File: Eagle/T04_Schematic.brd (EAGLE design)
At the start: 40.6 x 63.5 mm, 30 parts

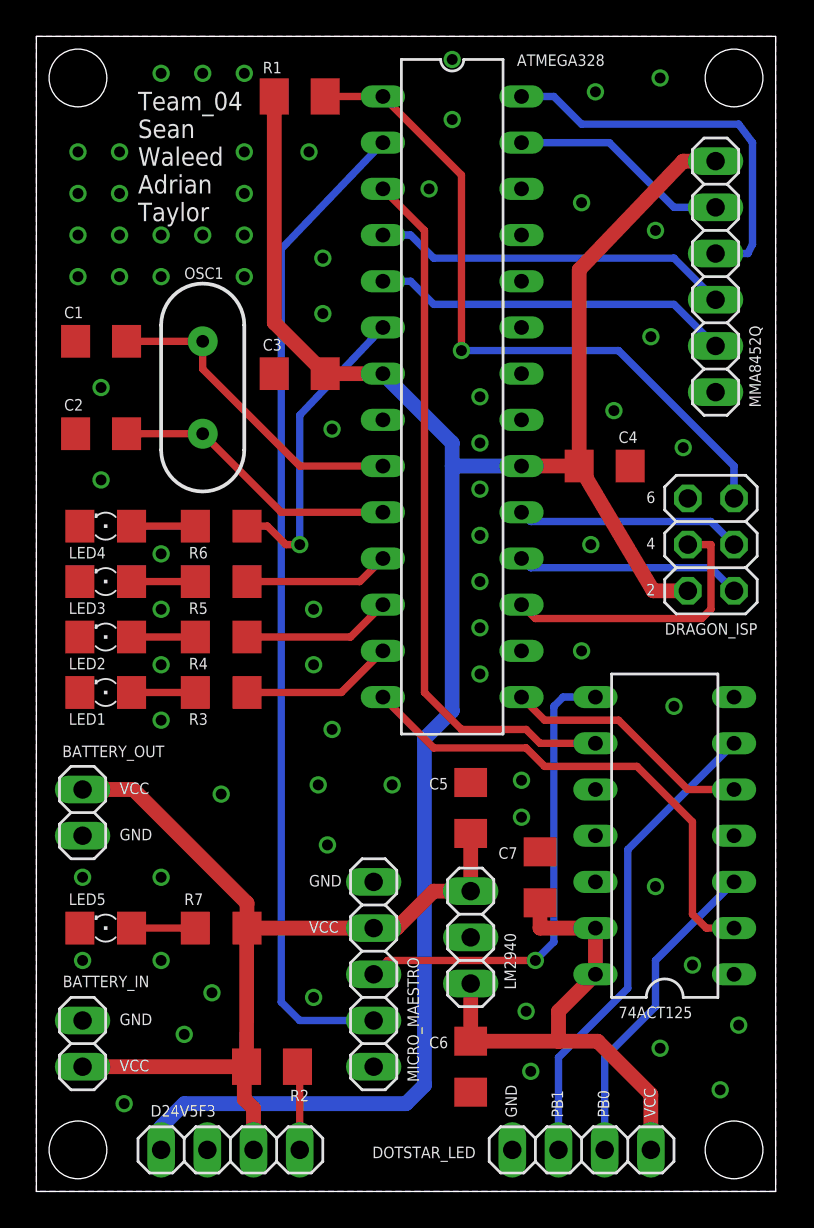
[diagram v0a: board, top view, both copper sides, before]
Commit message: Minor Changes for OSHPark -- PRINTED
Moved vias and text to make it pretty.
-- This File Uploaded to Print!!!
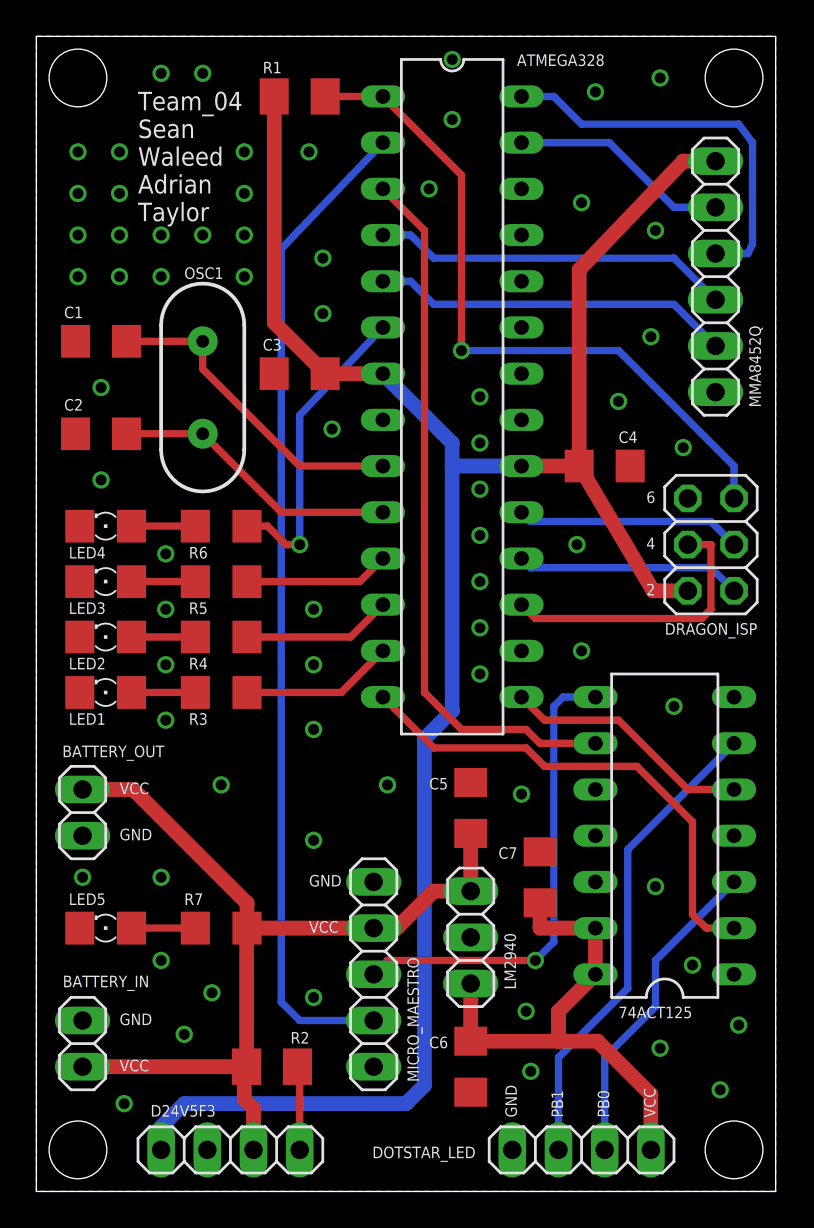
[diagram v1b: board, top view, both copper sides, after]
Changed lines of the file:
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@@
 </element>
 <element name="R2" library="rcl" package="M1206" value="10K" x="12.954" y="6.858" smashed="yes" rot="R180">
-<attribute name="NAME" x="14.986" y="5.588" size="0.635" layer="25" rot="R180"/>
+<attribute name="NAME" x="13.97" y="8.128" size="0.635" layer="25"/>
 <attribute name="VALUE" x="14.224" y="4.318" size="0.6096" layer="27"/>
 </element>
@@
 <via x="6.858" y="61.468" extent="1-16" drill="0.6"/>
 <via x="9.144" y="61.468" extent="1-16" drill="0.6"/>
-<via x="11.43" y="61.468" extent="1-16" drill="0.6"/>
+<wire x1="11.43" y1="61.468" x2="11.43" y2="61.468" width="0" layer="19" extent="1-16"/>
 <via x="11.43" y="50.292" extent="1-16" drill="0.6"/>
 <via x="3.556" y="44.196" extent="1-16" drill="0.6"/>
 <via x="3.556" y="39.116" extent="1-16" drill="0.6"/>
-<via x="6.858" y="35.052" extent="1-16" drill="0.6"/>
-<via x="6.858" y="32.004" extent="1-16" drill="0.6"/>
-<via x="6.858" y="28.956" extent="1-16" drill="0.6"/>
-<via x="6.858" y="25.908" extent="1-16" drill="0.6"/>
+<via x="7.112" y="35.052" extent="1-16" drill="0.6"/>
+<via x="7.112" y="32.004" extent="1-16" drill="0.6"/>
+<via x="7.112" y="28.956" extent="1-16" drill="0.6"/>
+<via x="7.112" y="25.908" extent="1-16" drill="0.6"/>
 <via x="2.54" y="17.272" extent="1-16" drill="0.6"/>
-<via x="2.54" y="12.7" extent="1-16" drill="0.6"/>
+<wire x1="2.54" y1="12.7" x2="2.54" y2="12.7" width="0" layer="19" extent="1-16"/>
 <via x="6.858" y="17.272" extent="1-16" drill="0.6"/>
 <via x="6.858" y="12.7" extent="1-16" drill="0.6"/>
@@
 <via x="26.924" y="9.906" extent="1-16" drill="0.6"/>
 <via x="37.592" y="5.588" extent="1-16" drill="0.6"/>
-<via x="10.16" y="21.844" extent="1-16" drill="0.6"/>
-<via x="19.558" y="22.352" extent="1-16" drill="0.6"/>
+<via x="10.16" y="22.352" extent="1-16" drill="0.6"/>
+<via x="19.304" y="22.352" extent="1-16" drill="0.6"/>
 <via x="24.384" y="41.148" extent="1-16" drill="0.6"/>
-<via x="31.75" y="42.926" extent="1-16" drill="0.6"/>
-<via x="30.48" y="35.56" extent="1-16" drill="0.6"/>
+<via x="32.004" y="43.434" extent="1-16" drill="0.6"/>
+<via x="29.718" y="35.56" extent="1-16" drill="0.6"/>
 <via x="33.782" y="46.99" extent="1-16" drill="0.6"/>
 <via x="29.972" y="54.356" extent="1-16" drill="0.6"/>
@@
 <via x="15.24" y="32.004" extent="1-16" drill="0.6"/>
 <via x="15.24" y="28.956" extent="1-16" drill="0.6"/>
-<via x="16.256" y="25.4" extent="1-16" drill="0.6"/>
+<via x="15.24" y="25.4" extent="1-16" drill="0.6"/>
 <via x="15.24" y="10.668" extent="1-16" drill="0.6"/>
-<via x="16.002" y="19.05" extent="1-16" drill="0.6"/>
+<via x="15.24" y="19.304" extent="1-16" drill="0.6"/>
 <contactref element="74ACT125" pad="11"/>
 <contactref element="74ACT125" pad="12"/>
@@
 <via x="34.036" y="52.832" extent="1-16" drill="0.6"/>
 <via x="21.59" y="55.118" extent="1-16" drill="0.6"/>
-<via x="15.494" y="22.352" extent="1-16" drill="0.6"/>
-<via x="26.67" y="20.574" extent="1-16" drill="0.6"/>
+<wire x1="15.24" y1="22.352" x2="15.24" y2="22.352" width="0" layer="19" extent="1-16"/>
+<wire x1="26.67" y1="20.574" x2="26.67" y2="20.574" width="0" layer="19" extent="1-16"/>
 <via x="35.052" y="26.67" extent="1-16" drill="0.6"/>
 <via x="34.036" y="16.764" extent="1-16" drill="0.6"/>
 <via x="38.608" y="9.144" extent="1-16" drill="0.6"/>
-<via x="26.67" y="22.606" extent="1-16" drill="0.6"/>
+<via x="26.67" y="21.844" extent="1-16" drill="0.6"/>
 <contactref element="C7" pad="2"/>
 <via x="34.29" y="7.874" extent="1-16" drill="0.6"/>

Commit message: Added Resistor and LED Voltages
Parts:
- LED1: value TBD Voltage -> G - 2.1V
- LED2, LED3: value TBD Voltage -> Y - 2.2V
- LED4: value TBD Voltage -> R - 1.7V
- LED5: value TBD Voltage -> B - 3.2V
- R3: value TBD Resistance -> 68 Ohms
- R4, R5: value TBD Resistance -> 56 Ohms
- R6: value TBD Resistance -> 82 Ohms
- R7: value TBD Resistance -> 150 Ohms
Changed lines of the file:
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@@
 <attribute name="NAME" x="34.544" y="30.607" size="0.635" layer="25" ratio="10"/>
 </element>
-<element name="LED1" library="led" package="1206" value="TBD Voltage" x="3.81" y="27.432" smashed="yes" rot="R180">
+<element name="LED1" library="led" package="1206" value="G - 2.1V" x="3.81" y="27.432" smashed="yes" rot="R180">
 <attribute name="NAME" x="1.778" y="25.654" size="0.635" layer="25"/>
 </element>
-<element name="LED2" library="led" package="1206" value="TBD Voltage" x="3.81" y="30.48" smashed="yes" rot="R180">
+<element name="LED2" library="led" package="1206" value="Y - 2.2V" x="3.81" y="30.48" smashed="yes" rot="R180">
 <attribute name="NAME" x="1.778" y="28.702" size="0.635" layer="25"/>
 </element>
-<element name="LED3" library="led" package="1206" value="TBD Voltage" x="3.81" y="33.528" smashed="yes" rot="R180">
+<element name="LED3" library="led" package="1206" value="Y - 2.2V" x="3.81" y="33.528" smashed="yes" rot="R180">
 <attribute name="NAME" x="1.778" y="31.75" size="0.635" layer="25"/>
 </element>
-<element name="LED4" library="led" package="1206" value="TBD Voltage" x="3.81" y="36.576" smashed="yes" rot="R180">
+<element name="LED4" library="led" package="1206" value="R - 1.7V" x="3.81" y="36.576" smashed="yes" rot="R180">
 <attribute name="NAME" x="1.778" y="34.798" size="0.635" layer="25"/>
 </element>
-<element name="LED5" library="led" package="1206" value="TBD Voltage" x="3.81" y="14.478" smashed="yes" rot="R180">
+<element name="LED5" library="led" package="1206" value="B - 3.2V" x="3.81" y="14.478" smashed="yes" rot="R180">
 <attribute name="NAME" x="1.778" y="15.748" size="0.635" layer="25"/>
 </element>
-<element name="R3" library="rcl" package="R1206" value="TBD Resistance" x="10.16" y="27.432" smashed="yes" rot="R180">
+<element name="R3" library="rcl" package="R1206" value="68 Ohms" x="10.16" y="27.432" smashed="yes" rot="R180">
 <attribute name="NAME" x="8.382" y="25.654" size="0.635" layer="25"/>
 <attribute name="VALUE" x="11.43" y="29.972" size="1.27" layer="27" rot="R180"/>
 </element>
-<element name="R4" library="rcl" package="R1206" value="TBD Resistance" x="10.16" y="30.48" smashed="yes" rot="R180">
+<element name="R4" library="rcl" package="R1206" value="56 Ohms" x="10.16" y="30.48" smashed="yes" rot="R180">
 <attribute name="NAME" x="8.382" y="28.702" size="0.635" layer="25"/>
 <attribute name="VALUE" x="11.43" y="33.02" size="1.27" layer="27" rot="R180"/>
 </element>
-<element name="R5" library="rcl" package="R1206" value="TBD Resistance" x="10.16" y="33.528" smashed="yes" rot="R180">
+<element name="R5" library="rcl" package="R1206" value="56 Ohms" x="10.16" y="33.528" smashed="yes" rot="R180">
 <attribute name="NAME" x="8.382" y="31.75" size="0.635" layer="25"/>
 <attribute name="VALUE" x="11.43" y="36.068" size="1.27" layer="27" rot="R180"/>
 </element>
-<element name="R6" library="rcl" package="R1206" value="TBD Resistance" x="10.16" y="36.576" smashed="yes" rot="R180">
+<element name="R6" library="rcl" package="R1206" value="82 Ohms" x="10.16" y="36.576" smashed="yes" rot="R180">
 <attribute name="NAME" x="8.382" y="34.798" size="0.635" layer="25"/>
 <attribute name="VALUE" x="11.43" y="39.116" size="1.27" layer="27" rot="R180"/>
 </element>
-<element name="R7" library="rcl" package="R1206" value="TBD Resistance" x="10.16" y="14.478" smashed="yes" rot="R180">
+<element name="R7" library="rcl" package="R1206" value="150 Ohms" x="10.16" y="14.478" smashed="yes" rot="R180">
 <attribute name="NAME" x="8.128" y="15.748" size="0.635" layer="25"/>
 <attribute name="VALUE" x="11.43" y="17.018" size="1.27" layer="27" rot="R180"/>
